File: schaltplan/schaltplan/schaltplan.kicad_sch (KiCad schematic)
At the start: 1 part, among them U1 DFR0478

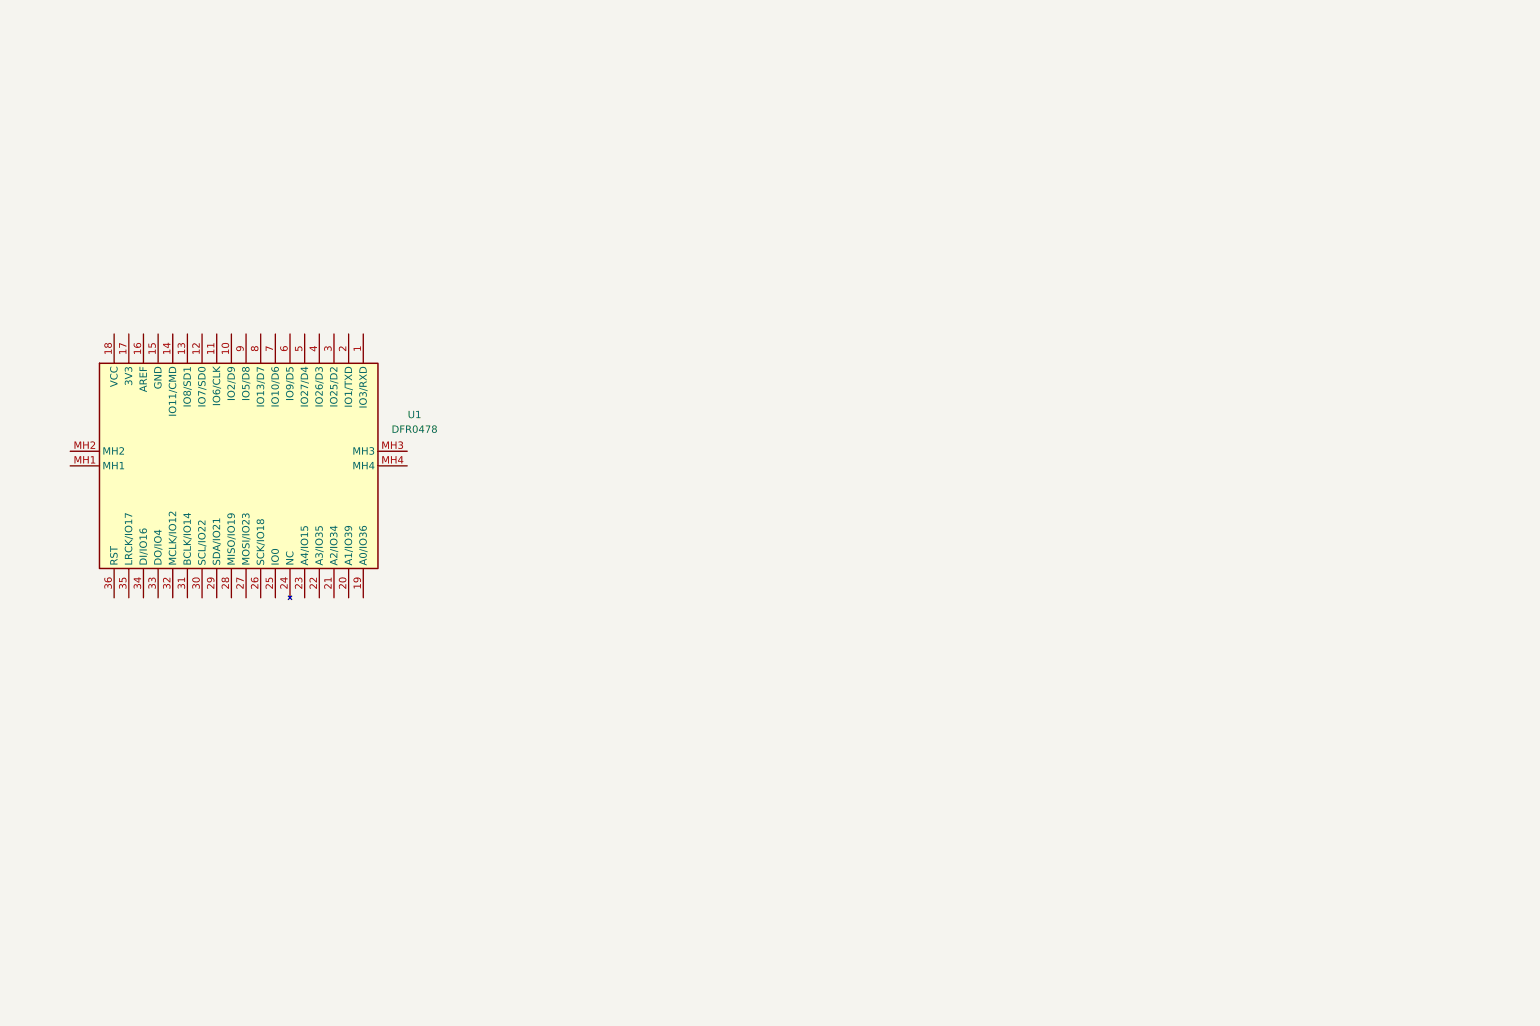
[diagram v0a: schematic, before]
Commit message: display und LEDS auf dem schaltplan eingezeichnet
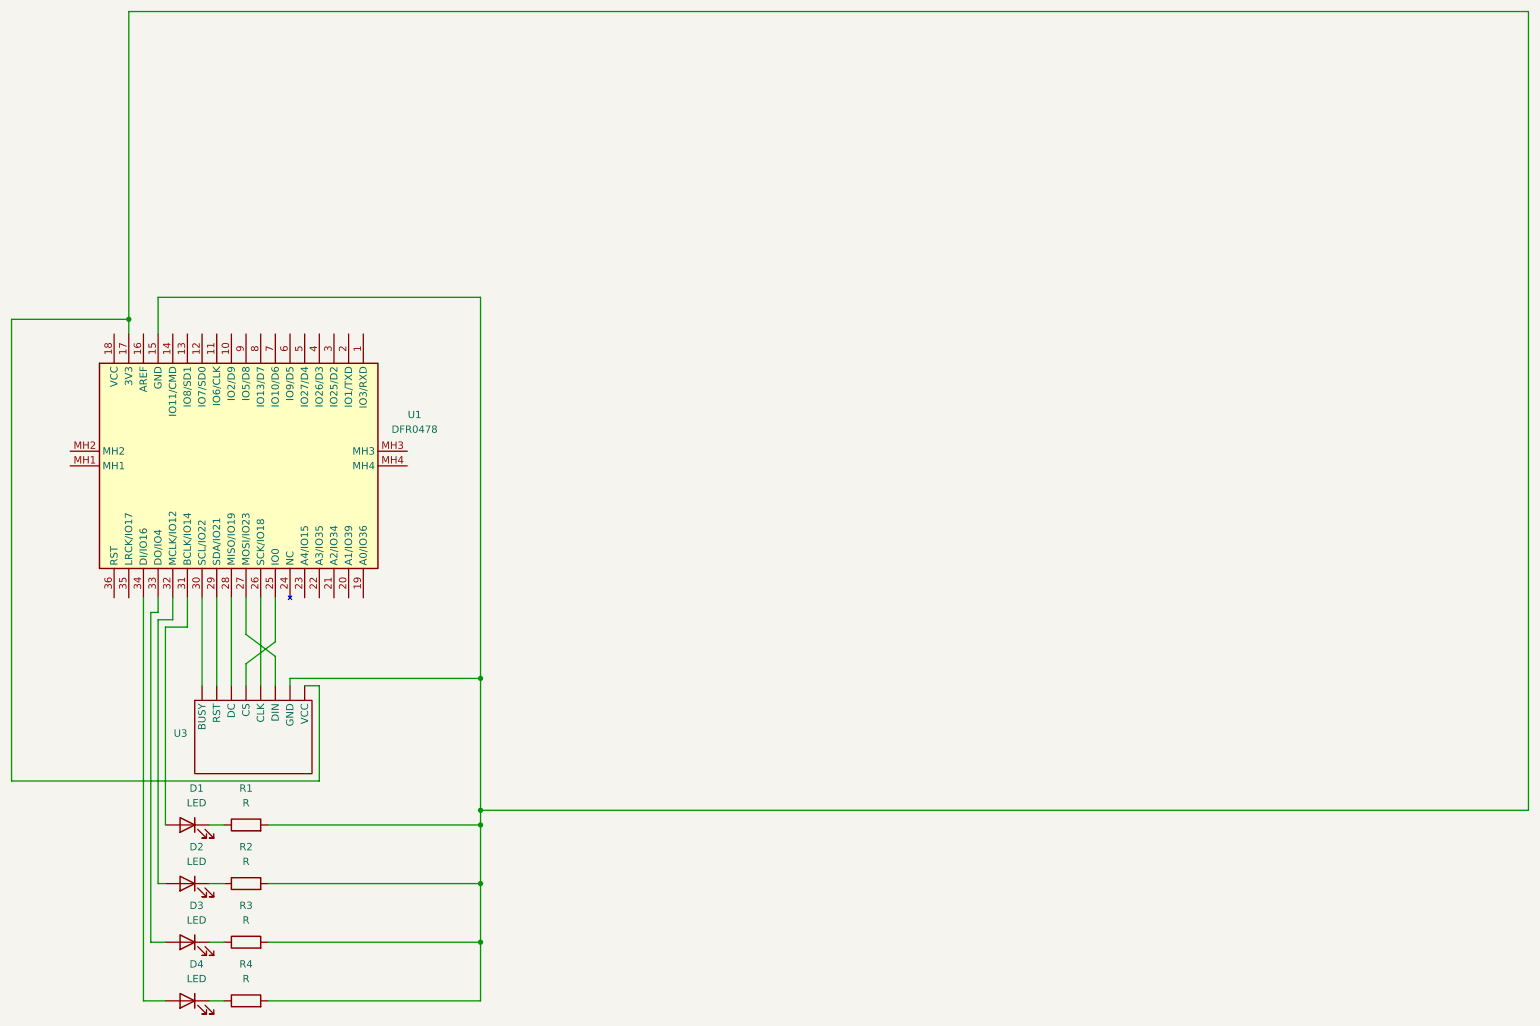
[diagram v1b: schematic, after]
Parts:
- added D1, D2, D3, D4: LED, symbol Device:LED
- added R1, R2, R3, R4: R, symbol Device:R
- added U3: ~, symbol video:waveshare_2.9
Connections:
- net at U1.15 (GND): now also U1.17 (3V3), R1.2, R2.2, R3.2, R4.2, U3. (VCC)
- net at U1.25 (IO0): now also U3. (VCC)
- net at U1.26 (SCK/IO18): now also U3. (VCC)
- net at U1.27 (MOSI/IO23): now also U3. (VCC)
- net at U1.28 (MISO/IO19): now also U3. (VCC)
- net at U1.29 (SDA/IO21): now also U3. (VCC)
- net at U1.30 (SCL/IO22): now also U3. (VCC)
- net at U1.31 (BCLK/IO14): now also D1.2 (A)
- net at U1.32 (MCLK/IO12): now also D2.2 (A)
- net at U1.33 (DO/IO4): now also D3.2 (A)
- net at U1.34 (DI/IO16): now also D4.2 (A)
- new net: D3.1 (K), R3.1
- new net: D2.1 (K), R2.1
- new net: D1.1 (K), R1.1
- new net: D4.1 (K), R4.1

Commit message: leds verschoben und an/aus schalter eingezeichnet
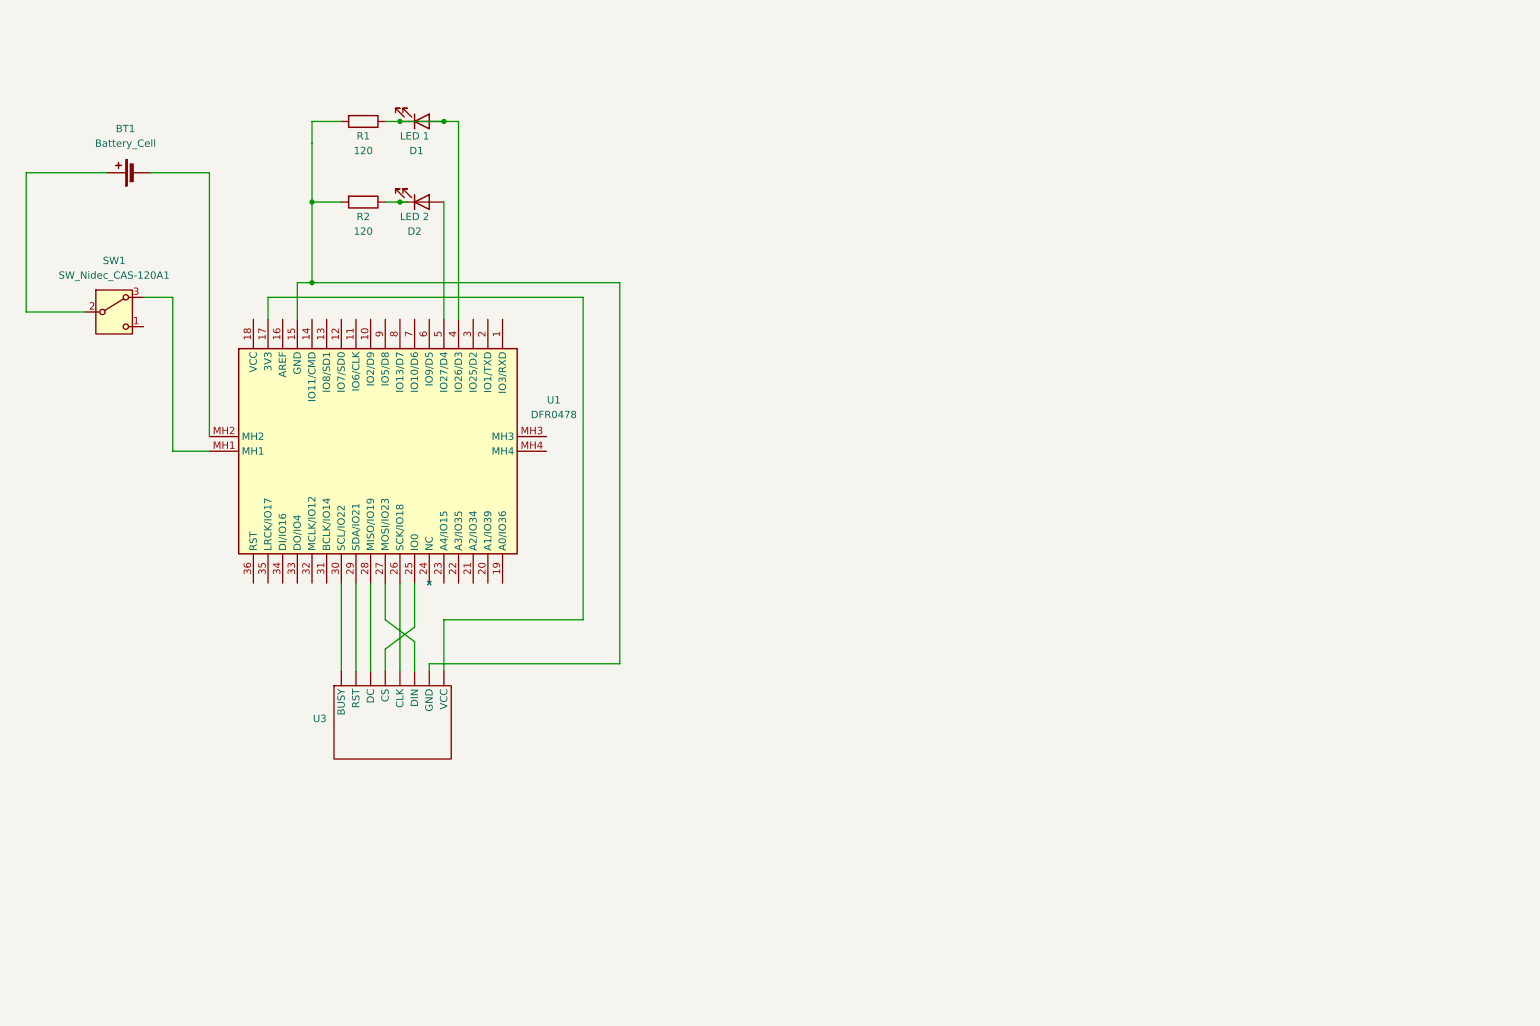
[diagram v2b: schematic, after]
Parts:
- removed D3, D4: LED, symbol Device:LED
- removed R3, R4: R, symbol Device:R
- added BT1: Battery_Cell, symbol Device:Battery_Cell
- added SW1: SW_Nidec_CAS-120A1, Button_Switch_SMD:Nidec_Copal_CAS-120A, symbol Switch:SW_Nidec_CAS-120A1
- D1: renamed from D2; value LED -> LED 1
- D2: renamed from D1; value LED -> LED 2
- R1: renamed from R2; value R -> 120
- R2: renamed from R1; value R -> 120
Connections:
- net at D1.1 (K), R1.1: now also D1.2 (A), U1.4 (IO26/D3)
- net at U1.32 (MCLK/IO12): no longer D1.2 (A)
- net at D2.2 (A): now also U1.5 (IO27/D4); no longer U1.31 (BCLK/IO14)
- net at R1.2, R2.2, U1.15 (GND)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: no longer U1.17 (3V3)
- net at U1.MH1: now also SW1.3 (A)
- net at U1.MH2: now also BT1.2 (-)
- new net: BT1.1 (+), SW1.2 (B)
- new net: U1.17 (3V3), U3. (VCC)
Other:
- moved on the sheet: D1, D2, R1, R2, U1, U3

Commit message: kleine aktualisierung der ausrichtung einer beschriftung
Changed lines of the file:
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@@
 		(dnp no)
 		(property "Reference" "U3"
-			(at 69.85 145.4149 90)
+			(at 69.342 143.002 0)
 			(effects
 				(font
@@
 		(pin "23"
 		)
-		(pin "MH4"
-		)
 		(pin "12"
 		)
@@
 		(pin "MH2"
 		)
-		(pin "MH3"
-		)
 		(pin "15"

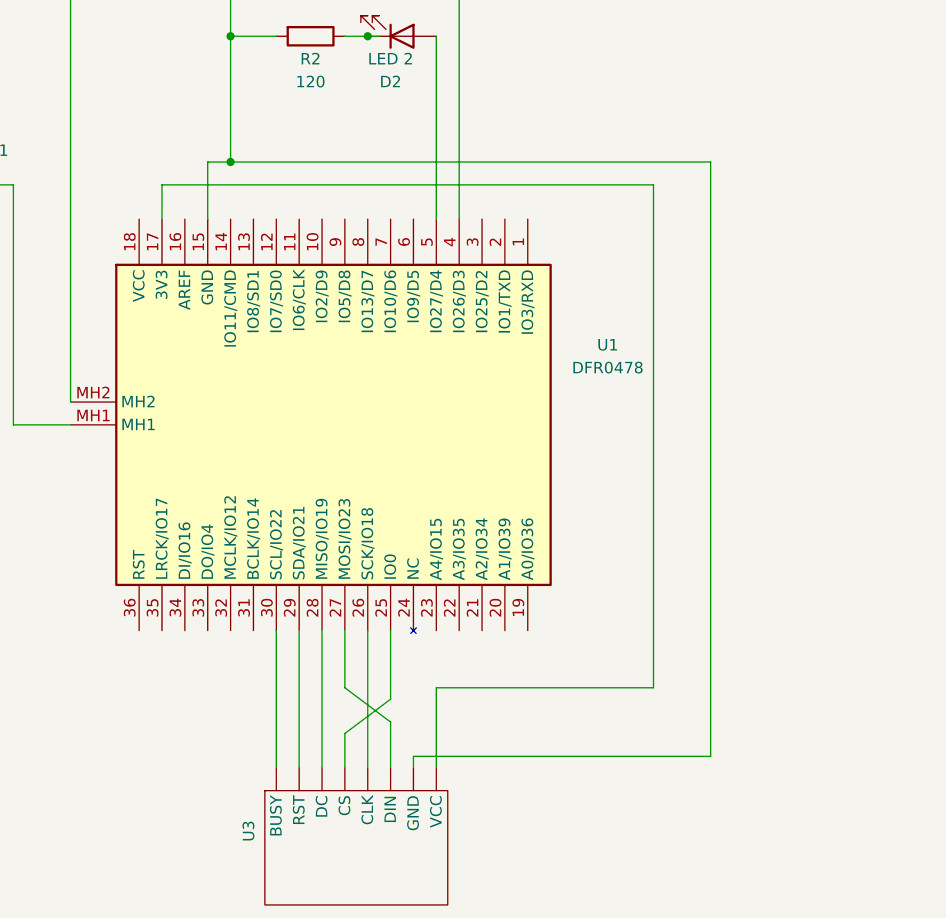
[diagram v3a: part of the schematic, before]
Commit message: potentiometer auf schaltplan ergänzt sowie code um potentiometer ergänzt
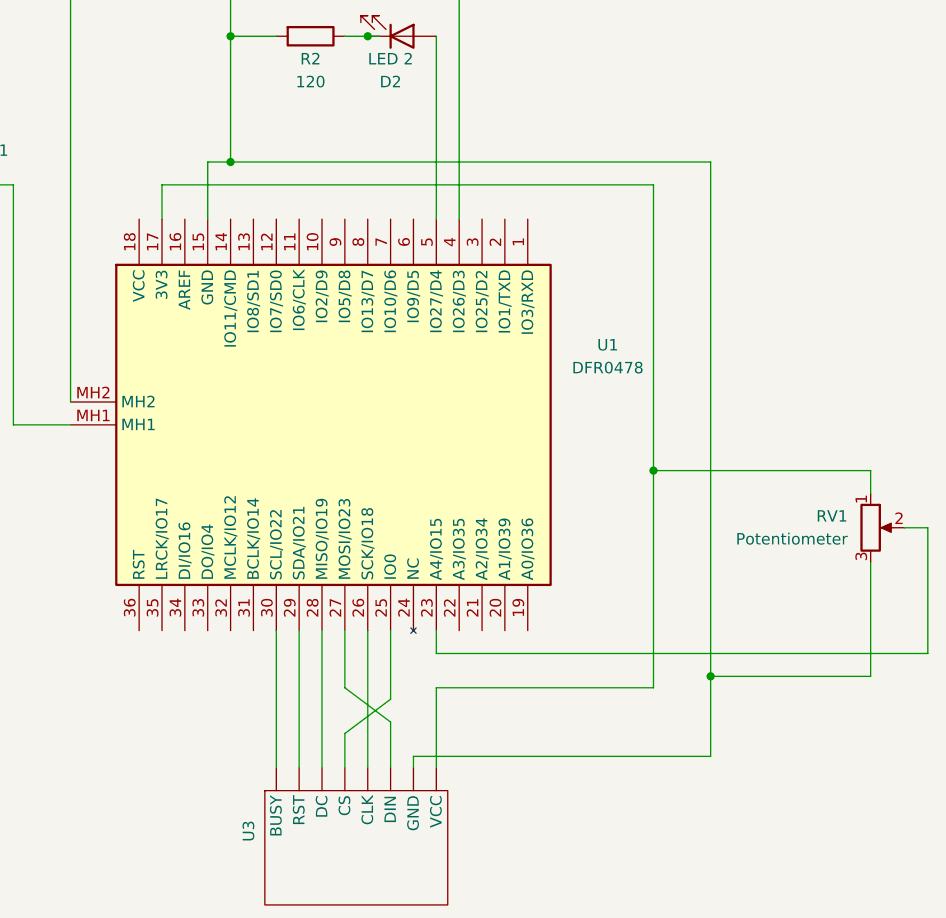
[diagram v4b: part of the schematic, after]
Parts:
- added RV1: Potentiometer, symbol Device:R_Potentiometer
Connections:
- net at R1.2, R2.2, U1.15 (GND)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: now also RV1.3
- net at U1.17 (3V3), U3. (VCC): now also RV1.1
- net at U1.23 (A4/IO15): now also RV1.2
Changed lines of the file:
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@@
+	)
+	(junction
+		(at 114.3 104.14)
+		(diameter 0)
+		(color 0 0 0 0)
+	)
+	(junction
+		(at 120.65 127)
+		(diameter 0)
+		(color 0 0 0 0)
 	)
 	(junction
@@
 	(wire
 		(pts
+			(xy 142.24 110.49) (xy 144.78 110.49)
+		)
+		(stroke
+			(width 0)
+			(type default)
+		)
+	)
+	(wire
+		(pts
+			(xy 114.3 104.14) (xy 138.43 104.14)
+		)
+		(stroke
+			(width 0)
+			(type default)
+			(color 255 0 9 1)
+		)
+	)
+	(wire
+		(pts
 			(xy 67.31 55.88) (xy 67.31 69.85)
 		)
@@
 	(wire
 		(pts
-			(xy 120.65 69.85) (xy 120.65 135.89)
+			(xy 90.17 121.92) (xy 90.17 124.46)
+		)
+		(stroke
+			(width 0)
+			(type default)
+		)
+	)
+	(wire
+		(pts
+			(xy 138.43 114.3) (xy 138.43 127)
 		)
 		(stroke
@@
 	(wire
 		(pts
+			(xy 138.43 104.14) (xy 138.43 106.68)
+		)
+		(stroke
+			(width 0)
+			(type default)
+			(color 255 0 9 1)
+		)
+	)
+	(wire
+		(pts
 			(xy 64.77 69.85) (xy 64.77 76.2)
 		)
@@
 	(wire
 		(pts
-			(xy 114.3 72.39) (xy 114.3 128.27)
+			(xy 120.65 127) (xy 120.65 69.85)
+		)
+		(stroke
+			(width 0)
+			(type default)
+			(color 0 0 0 1)
+		)
+	)
+	(wire
+		(pts
+			(xy 59.69 72.39) (xy 59.69 76.2)
 		)
 		(stroke
@@
 	(wire
 		(pts
-			(xy 59.69 72.39) (xy 59.69 76.2)
+			(xy 120.65 127) (xy 138.43 127)
+		)
+		(stroke
+			(width 0)
+			(type default)
+			(color 0 0 0 1)
+		)
+	)
+	(wire
+		(pts
+			(xy 59.69 72.39) (xy 114.3 72.39)
 		)
 		(stroke
@@
 	(wire
 		(pts
-			(xy 114.3 72.39) (xy 59.69 72.39)
+			(xy 31.75 50.8) (xy 17.78 50.8)
+		)
+		(stroke
+			(width 0)
+			(type default)
+		)
+	)
+	(wire
+		(pts
+			(xy 72.39 121.92) (xy 72.39 137.16)
+		)
+		(stroke
+			(width 0)
+			(type default)
+		)
+	)
+	(wire
+		(pts
+			(xy 17.78 74.93) (xy 27.94 74.93)
+		)
+		(stroke
+			(width 0)
+			(type default)
+		)
+	)
+	(wire
+		(pts
+			(xy 74.93 121.92) (xy 74.93 137.16)
+		)
+		(stroke
+			(width 0)
+			(type default)
+		)
+	)
+	(wire
+		(pts
+			(xy 85.09 129.54) (xy 85.09 121.92)
+		)
+		(stroke
+			(width 0)
+			(type default)
+		)
+	)
+	(wire
+		(pts
+			(xy 114.3 72.39) (xy 114.3 104.14)
 		)
 		(stroke
@@
 	(wire
 		(pts
-			(xy 31.75 50.8) (xy 17.78 50.8)
-		)
-		(stroke
-			(width 0)
-			(type default)
-		)
-	)
-	(wire
-		(pts
-			(xy 72.39 121.92) (xy 72.39 137.16)
-		)
-		(stroke
-			(width 0)
-			(type default)
-		)
-	)
-	(wire
-		(pts
-			(xy 17.78 74.93) (xy 27.94 74.93)
-		)
-		(stroke
-			(width 0)
-			(type default)
-		)
-	)
-	(wire
-		(pts
-			(xy 74.93 121.92) (xy 74.93 137.16)
-		)
-		(stroke
-			(width 0)
-			(type default)
-		)
-	)
-	(wire
-		(pts
-			(xy 85.09 129.54) (xy 85.09 121.92)
-		)
-		(stroke
-			(width 0)
-			(type default)
+			(xy 114.3 104.14) (xy 114.3 128.27)
+		)
+		(stroke
+			(width 0)
+			(type default)
+			(color 255 0 9 1)
 		)
 	)
@@
 	(wire
 		(pts
+			(xy 90.17 124.46) (xy 144.78 124.46)
+		)
+		(stroke
+			(width 0)
+			(type default)
+		)
+	)
+	(wire
+		(pts
 			(xy 120.65 135.89) (xy 87.63 135.89)
 		)
@@
 	(wire
 		(pts
+			(xy 144.78 124.46) (xy 144.78 110.49)
+		)
+		(stroke
+			(width 0)
+			(type default)
+		)
+	)
+	(wire
+		(pts
 			(xy 38.1 72.39) (xy 43.18 72.39)
 		)
@@
 			(width 0)
 			(type default)
+		)
+	)
+	(wire
+		(pts
+			(xy 120.65 127) (xy 120.65 135.89)
+		)
+		(stroke
+			(width 0)
+			(type default)
+			(color 0 0 0 1)
 		)
 	)
@@
 					(unit 1)
 				)
+			)
+		)
+	)
+	(symbol
+		(lib_id "Device:R_Potentiometer")
+		(at 138.43 110.49 0)
+		(unit 1)
+		(exclude_from_sim no)
+		(in_bom yes)
+		(on_board yes)
+		(dnp no)
+		(fields_autoplaced yes)
+		(property "Reference" "RV1"
+			(at 135.89 109.2199 0)
+			(effects
+				(font
+					(size 1.27 1.27)
+				)
+				(justify right)
+			)
+		)
+		(property "Value" "Potentiometer"
+			(at 135.89 111.7599 0)
+			(effects
+				(font
+					(size 1.27 1.27)
+				)
+				(justify right)
+			)
+		)
+		(property "Footprint" ""
+			(at 138.43 110.49 0)
+			(effects
+				(font
+					(size 1.27 1.27)
+				)
+				(hide yes)
+			)
+		)
+		(property "Datasheet" "~"
+			(at 138.43 110.49 0)
+			(effects
+				(font
+					(size 1.27 1.27)
+				)
+				(hide yes)
+			)
+		)
+		(property "Description" "Potentiometer"
+			(at 138.43 110.49 0)
+			(effects
+				(font
+					(size 1.27 1.27)
+				)
+				(hide yes)
+			)
+		)
+		(pin "2"
+		)
+		(pin "1"
+		)
+		(pin "3"
+		)
+		(instances
+			(project ""
+				(path "/f79f94d7-572e-4250-b494-96d40f946eb3"
+					(reference "RV1")
+					(unit 1)
+				)
